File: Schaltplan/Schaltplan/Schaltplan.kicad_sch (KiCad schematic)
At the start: 32 parts, among them J1 Raspberry Pi Pico, M1 Motor_DC, M2 Motor_DC, M3 Motor_DC, M4 Motor_DC, M5 Motor_DC, Q1 IRLZ44N, Q2 IRLZ44N, Q3 IRLZ44N, Q4 IRLZ44N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

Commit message: j
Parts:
- removed R11: 10k, symbol Device:R
- R10, R6, R7, R8, R9: value 1k -> 330
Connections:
- net +12V: now also D1.1 (K), D2.1 (K), D3.1 (K), D4.1 (K), D5.1 (K); no longer D1.2 (A), D2.2 (A), D3.2 (A), D4.2 (A), D5.2 (A)
- net GND: now also J1.18 (Pin_35), Q1.3 (S), Q2.2 (D), Q3.2 (D), Q4.2 (D), Q5.2 (D), SW_Füllstand_1.2 (B), SW_Füllstand_2.2 (B), SW_Füllstand_3.2 (B), SW_Füllstand_4.2 (B), SW_Füllstand_5.2 (B)
- net at R1.1, R2.1, R3.1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: now also J1.36 (Pin_10); no longer J1.39 (Pin_4)
- net at M3.2 (-), Q3.1 (G): now also D3.2 (A); no longer D3.1 (K)
- net at M5.2 (-), Q5.1 (G): now also D5.2 (A); no longer D5.1 (K)
- net at M2.2 (-), Q2.1 (G): now also D2.2 (A); no longer D2.1 (K)
- net at M4.2 (-), Q4.1 (G): now also D4.2 (A); no longer D4.1 (K)
- net at R6.2: now also Q1.1 (G); no longer Q1.3 (S)
- new net: D1.2 (A), M1.2 (-), Q1.2 (D)
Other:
- moved on the sheet: D1, D2, D3, D4, D5, Q1
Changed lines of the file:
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@@
 	)
 	(junction
+		(at 180.34 71.12)
+		(diameter 0)
+		(color 0 0 0 0)
+	)
+	(junction
 		(at 267.97 20.32)
 		(diameter 0)
@@
 	)
 	(junction
-		(at 180.34 71.12)
-		(diameter 0)
-		(color 0 0 0 0)
-	)
-	(junction
 		(at 270.51 20.32)
 		(diameter 0)
@@
 	(wire
 		(pts
-			(xy 165.1 38.1) (xy 224.79 38.1)
+			(xy 167.64 38.1) (xy 224.79 38.1)
 		)
 		(stroke
@@
 	(wire
 		(pts
+			(xy 110.49 52.07) (xy 118.11 52.07)
+		)
+		(stroke
+			(width 0)
+			(type default)
+		)
+	)
+	(wire
+		(pts
 			(xy 180.34 129.54) (xy 180.34 151.13)
 		)
@@
 	(wire
 		(pts
+			(xy 170.18 71.12) (xy 180.34 71.12)
+		)
+		(stroke
+			(width 0)
+			(type default)
+		)
+	)
+	(wire
+		(pts
 			(xy 19.05 59.69) (xy 19.05 74.93)
 		)
@@
 	(wire
 		(pts
-			(xy 227.33 62.23) (xy 165.1 62.23)
+			(xy 167.64 53.34) (xy 167.64 52.07)
 		)
 		(stroke
@@
 	(wire
 		(pts
-			(xy 121.92 80.01) (xy 121.92 129.54)
+			(xy 227.33 62.23) (xy 165.1 62.23)
 		)
 		(stroke
@@
 	(wire
 		(pts
-			(xy 19.05 25.4) (xy 19.05 41.91)
+			(xy 121.92 80.01) (xy 121.92 129.54)
 		)
 		(stroke
@@
 	(wire
 		(pts
-			(xy 240.03 119.38) (xy 240.03 116.84)
+			(xy 19.05 25.4) (xy 19.05 41.91)
 		)
 		(stroke
@@
 	(wire
 		(pts
-			(xy 240.03 119.38) (xy 223.52 119.38)
+			(xy 240.03 119.38) (xy 240.03 116.84)
 		)
 		(stroke
@@
 	(wire
 		(pts
-			(xy 227.33 45.72) (xy 227.33 49.53)
+			(xy 240.03 119.38) (xy 223.52 119.38)
 		)
 		(stroke
@@
 	(wire
 		(pts
-			(xy 110.49 44.45) (xy 118.11 44.45)
+			(xy 227.33 45.72) (xy 227.33 49.53)
 		)
 		(stroke
@@
 	(wire
 		(pts
-			(xy 165.1 38.1) (xy 165.1 39.37)
+			(xy 167.64 38.1) (xy 167.64 41.91)
 		)
 		(stroke
@@
 	(wire
 		(pts
-			(xy 180.34 46.99) (xy 180.34 71.12)
+			(xy 180.34 53.34) (xy 180.34 71.12)
 		)
 		(stroke
@@
 	(wire
 		(pts
-			(xy 180.34 46.99) (xy 170.18 46.99)
+			(xy 180.34 53.34) (xy 167.64 53.34)
 		)
 		(stroke
@@
 	(wire
 		(pts
-			(xy 180.34 160.02) (xy 199.39 160.02)
+			(xy 180.34 160.02) (xy 246.38 160.02)
 		)
 		(stroke
@@
 	(wire
 		(pts
-			(xy 207.01 160.02) (xy 246.38 160.02)
-		)
-		(stroke
-			(width 0)
-			(type default)
-		)
-	)
-	(wire
-		(pts
 			(xy 224.79 38.1) (xy 240.03 38.1)
 		)
@@
 	(wire
 		(pts
-			(xy 118.11 44.45) (xy 118.11 25.4)
+			(xy 118.11 25.4) (xy 118.11 52.07)
 		)
 		(stroke
@@
 	(wire
 		(pts
-			(xy 180.34 71.12) (xy 170.18 71.12)
-		)
-		(stroke
-			(width 0)
-			(type default)
-		)
-	)
-	(wire
-		(pts
 			(xy 240.03 20.32) (xy 240.03 24.13)
 		)
@@
 	(symbol
 		(lib_id "Device:D")
-		(at 224.79 81.28 90)
+		(at 224.79 81.28 270)
 		(unit 1)
 		(exclude_from_sim no)
@@
 		(fields_autoplaced yes)
 		(property "Reference" "D3"
-			(at 218.44 81.28 0)
+			(at 227.33 80.0099 90)
 			(effects
 				(font
 					(size 1.27 1.27)
 				)
+				(justify left)
 			)
 		)
 		(property "Value" "D"
-			(at 220.98 81.28 0)
+			(at 227.33 82.5499 90)
 			(effects
 				(font
 					(size 1.27 1.27)
 				)
+				(justify left)
 			)
 		)
@@
 			)
 		)
-		(property "Value" "1k"
+		(property "Value" "330"
 			(at 138.43 67.31 90)
 			(effects
@@
 	(symbol
 		(lib_id "Device:D")
-		(at 222.25 134.62 90)
+		(at 222.25 134.62 270)
 		(unit 1)
 		(exclude_from_sim no)
@@
 		(fields_autoplaced yes)
 		(property "Reference" "D5"
-			(at 215.9 134.62 0)
+			(at 224.79 133.3499 90)
 			(effects
 				(font
 					(size 1.27 1.27)
 				)
+				(justify left)
 			)
 		)
 		(property "Value" "D"
-			(at 218.44 134.62 0)
+			(at 224.79 135.8899 90)
 			(effects
 				(font
 					(size 1.27 1.27)
 				)
+				(justify left)
 			)
 		)
@@
 	)
 	(symbol
-		(lib_id "Device:R")
-		(at 203.2 160.02 90)
-		(unit 1)
-		(exclude_from_sim no)
-		(in_bom yes)
-		(on_board yes)
-		(dnp no)
-		(fields_autoplaced yes)
-		(property "Reference" "R11"
-			(at 203.2 153.67 90)
-			(effects
-				(font
-					(size 1.27 1.27)
-				)
-			)
-		)
-		(property "Value" "10k"
-			(at 203.2 156.21 90)
-			(effects
-				(font
-					(size 1.27 1.27)
-				)
-			)
-		)
-		(property "Footprint" ""
-			(at 203.2 161.798 90)
-			(effects
-				(font
-					(size 1.27 1.27)
-				)
-				(hide yes)
-			)
-		)
-		(property "Datasheet" "~"
-			(at 203.2 160.02 0)
-			(effects
-				(font
-					(size 1.27 1.27)
-				)
-				(hide yes)
-			)
-		)
-		(property "Description" "Resistor"
-			(at 203.2 160.02 0)
-			(effects
-				(font
-					(size 1.27 1.27)
-				)
-				(hide yes)
-			)
-		)
-		(pin "2"
-		)
-		(pin "1"
-		)
-		(instances
-			(project "Schaltplan"
-				(path "/0e7ac635-20e1-4295-a698-68ba131a98e3"
-					(reference "R11")
-					(unit 1)
-				)
-			)
-		)
-	)
-	(symbol
 		(lib_id "Switch:SW_SPST")
 		(at 57.15 55.88 0)
@@
 			)
 		)
-		(property "Value" "1k"
+		(property "Value" "330"
 			(at 138.43 147.32 90)
 			(effects
@@
 			)
 		)
-		(property "Value" "1k"
+		(property "Value" "330"
 			(at 138.43 43.18 90)
 			(effects
@@
 	(symbol
 		(lib_id "Device:D")
-		(at 223.52 109.22 90)
+		(at 223.52 109.22 270)
 		(unit 1)
 		(exclude_from_sim no)
@@
 		(fields_autoplaced yes)
 		(property "Reference" "D4"
-			(at 217.17 109.22 0)
+			(at 226.06 107.9499 90)
 			(effects
 				(font
 					(size 1.27 1.27)
 				)
+				(justify left)
 			)
 		)
 		(property "Value" "D"
-			(at 219.71 109.22 0)
+			(at 226.06 110.4899 90)
 			(effects
 				(font
 					(size 1.27 1.27)
 				)
+				(justify left)
 			)
 		)
@@
 	(symbol
 		(lib_id "Device:D")
-		(at 227.33 53.34 90)
+		(at 227.33 53.34 270)
 		(unit 1)
 		(exclude_from_sim no)
@@
 		(fields_autoplaced yes)
 		(property "Reference" "D2"
-			(at 220.98 53.34 0)
+			(at 229.87 52.0699 90)
 			(effects
 				(font
 					(size 1.27 1.27)
 				)
+				(justify left)
 			)
 		)
 		(property "Value" "D"
-			(at 223.52 53.34 0)
+			(at 229.87 54.6099 90)
 			(effects
 				(font
 					(size 1.27 1.27)
 				)
+				(justify left)
 			)
 		)
@@
 	(symbol
 		(lib_id "Transistor_FET:IRLZ44N")
-		(at 165.1 44.45 270)
+		(at 165.1 46.99 0)
 		(unit 1)
 		(exclude_from_sim no)
@@
 		(fields_autoplaced yes)
 		(property "Reference" "Q1"
-			(at 165.1 50.8 90)
+			(at 171.45 45.7199 0)
 			(effects
 				(font
 					(size 1.27 1.27)
 				)
+				(justify left)
 			)
 		)
 		(property "Value" "IRLZ44N"
-			(at 165.1 53.34 90)
+			(at 171.45 48.2599 0)
 			(effects
 				(font
 					(size 1.27 1.27)
 				)
+				(justify left)
 			)
 		)
 		(property "Footprint" "Package_TO_SOT_THT:TO-220-3_Vertical"
-			(at 163.195 49.53 0)
+			(at 170.18 48.895 0)
 			(effects
 				(font
@@
 		)
 		(property "Datasheet" "http://www.irf.com/product-info/datasheets/data/irlz44n.pdf"
-			(at 161.29 49.53 0)
+			(at 170.18 50.8 0)
 			(effects
 				(font
@@
 		)
 		(property "Description" "47A Id, 55V Vds, 22mOhm Rds Single N-Channel HEXFET Power MOSFET, TO-220AB"
-			(at 165.1 44.45 0)
+			(at 165.1 46.99 0)
 			(effects
 				(font
@@
 			)
 		)
-		(property "Value" "1k"
+		(property "Value" "330"
 			(at 138.43 96.52 90)
 			(effects
@@
 			)
 		)
-		(property "Value" "1k"
+		(property "Value" "330"
 			(at 138.43 125.73 90)
 			(effects
@@
 	(symbol
 		(lib_id "Device:D")
-		(at 224.79 31.75 90)
+		(at 224.79 31.75 270)
 		(unit 1)
 		(exclude_from_sim no)
@@
 					(size 1.27 1.27)
 				)
-				(justify right)
+				(justify left)
 			)
 		)
@@
 					(size 1.27 1.27)
 				)
-				(justify right)
+				(justify left)
 			)
 		)

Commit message: hardware, mixer controller, rating
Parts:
- M1: value Motor_DC -> Wasser
- M2: value Motor_DC -> Sirup a
- M3: value Motor_DC -> Sirup b
- M4: value Motor_DC -> Sirup c
- M5: value Motor_DC -> Alkohol
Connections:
- net GND: now also Q2.3 (S), Q3.3 (S), Q4.3 (S), Q5.3 (S); no longer Q2.2 (D), Q3.2 (D), Q4.2 (D), Q5.2 (D)
- net at D3.2 (A), M3.2 (-): now also Q3.2 (D); no longer Q3.1 (G)
- net at R7.2: now also Q2.1 (G); no longer Q2.3 (S)
- net at D5.2 (A), M5.2 (-): now also Q5.2 (D); no longer Q5.1 (G)
- net at D2.2 (A), M2.2 (-): now also Q2.2 (D); no longer Q2.1 (G)
- net at R10.2: now also Q5.1 (G); no longer Q5.3 (S)
- net at R8.2: now also Q3.1 (G); no longer Q3.3 (S)
- net at D4.2 (A), M4.2 (-): now also Q4.2 (D); no longer Q4.1 (G)
- net at R9.2: now also Q4.1 (G); no longer Q4.3 (S)
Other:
- moved on the sheet: Q2, Q3, Q4, Q5, R9

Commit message: sensor test
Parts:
- removed J1: Raspberry Pi Pico, symbol Connector_Generic:Conn_02x20_Odd_Even
- removed SW_Füllstand_1, SW_Füllstand_2, SW_Füllstand_3, SW_Füllstand_4, SW_Füllstand_5: SW_SPST, symbol Switch:SW_SPST
- added C: Raspberry Pi Pico, symbol Connector_Generic:Conn_02x20_Odd_Even
- added H1, H2, H3, H4, H5: ~, symbol Connector_Generic_MountingPin:Conn_2Rows-11Pins_MountingPin
- added R11, R12, R13, R14, R15: 1kOhm, symbol Device:R
- added S1, S2, S3, S4, S5: Sensor, symbol Connector:Conn_01x04_Pin
- R1, R2, R3, R4, R5: value 10k -> 1kOhm
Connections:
- net GND: now also C.GND (Pin_36), H1.GND (Pin_2), H2.GND (Pin_2), H3.GND (Pin_2), H4.GND (Pin_2), H5.GND (Pin_2)
- net at R5.2: now also H3.A- (Pin_5), R11.2
- net at R1.2: now also R2.2, H1.A- (Pin_5)
- net at R10.1: now also C.GP18 (Pin_34)
- net at R9.1: now also C.GP19 (Pin_32)
- net at R8.1: now also C.GP20 (Pin_30)
- net at R7.1: now also C.GP21 (Pin_28)
- net at R6.1: now also C.GP22 (Pin_24)
- net at R3.2: now also R4.2, H2.A- (Pin_5)
- new net: H3.A+ (Pin_7), S3.RD (Pin_3)
- new net: C.GP3 (Pin_9), H3.DT (Pin_4)
- new net: H3.E+, H3.E- (Pin_3), R11.1, R5.1, S3.BL (Pin_2), S3.WH (Pin_1)
- new net: C.GP0 (Pin_1), H1.SCK (Pin_6), H2.SCK (Pin_6), H3.SCK (Pin_6), H4.SCK (Pin_6), H5.SCK (Pin_6)
- new net: C.3V3 (Pin_10), H1.VCC (Pin_8), H2.VCC (Pin_8), H3.VCC (Pin_8), H4.VCC (Pin_8), H5.VCC (Pin_8)
- new net: H5.E- (Pin_3), R14.1, S5.BL (Pin_2)
- new net: H5.A- (Pin_5), R14.2, R15.2
- new net: H4.E+, H4.E- (Pin_3), R12.1, R13.1, S4.BL (Pin_2), S4.WH (Pin_1)
- new net: H4.A- (Pin_5), R12.2, R13.2
- new net: H5.A+ (Pin_7), S5.RD (Pin_3)
- new net: H5.E+, R15.1, S5.WH (Pin_1)
- new net: H2.A+ (Pin_7), S2.RD (Pin_3)
- new net: C.GP2 (Pin_7), H2.DT (Pin_4)
- new net: H2.E+, R4.1, S2.WH (Pin_1)
- new net: H2.E- (Pin_3), R3.1, S2.BL (Pin_2)
- new net: H1.E+, R2.1, S1.WH (Pin_1)
- new net: H4.A+ (Pin_7), S4.RD (Pin_3)
- new net: H1.E- (Pin_3), R1.1, S1.BL (Pin_2)
- new net: H1.A+ (Pin_7), S1.RD (Pin_3)
- new net: C.GP1 (Pin_3), H1.DT (Pin_4)
- new net: C.GP15 (Pin_39), C.GP16 (Pin_40)
- new net: C.GP4 (Pin_11), H4.DT (Pin_4)
- new net: C.GP5 (Pin_13), H5.DT (Pin_4)

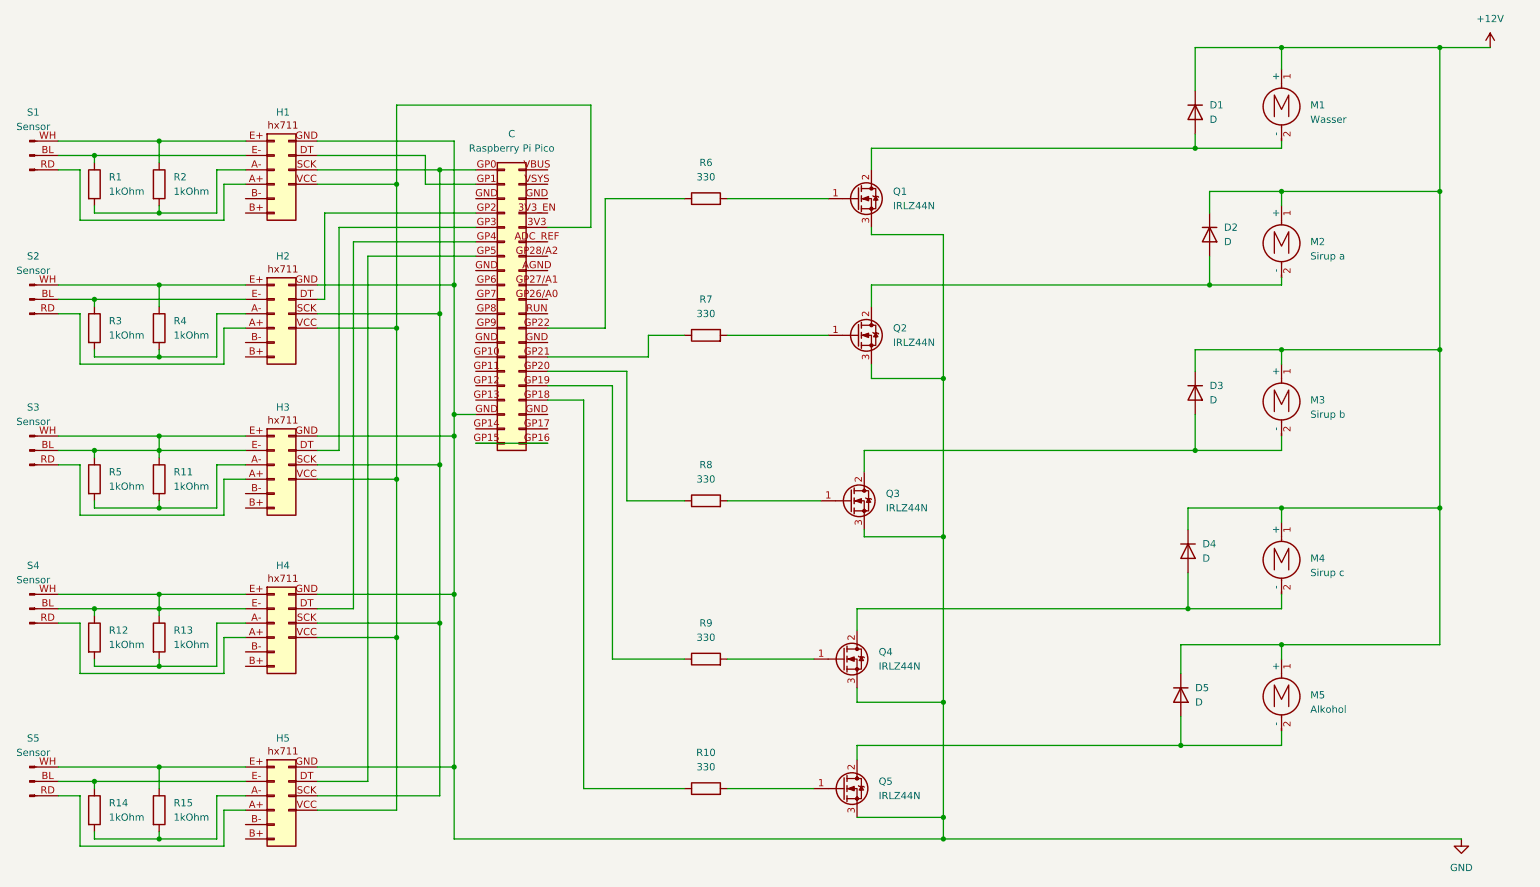
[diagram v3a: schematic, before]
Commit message: Implement basic functionality for beverage mixer including HX711 weight measurement and GPIO setup for pumps and sensors. Add initial test script for basic output.
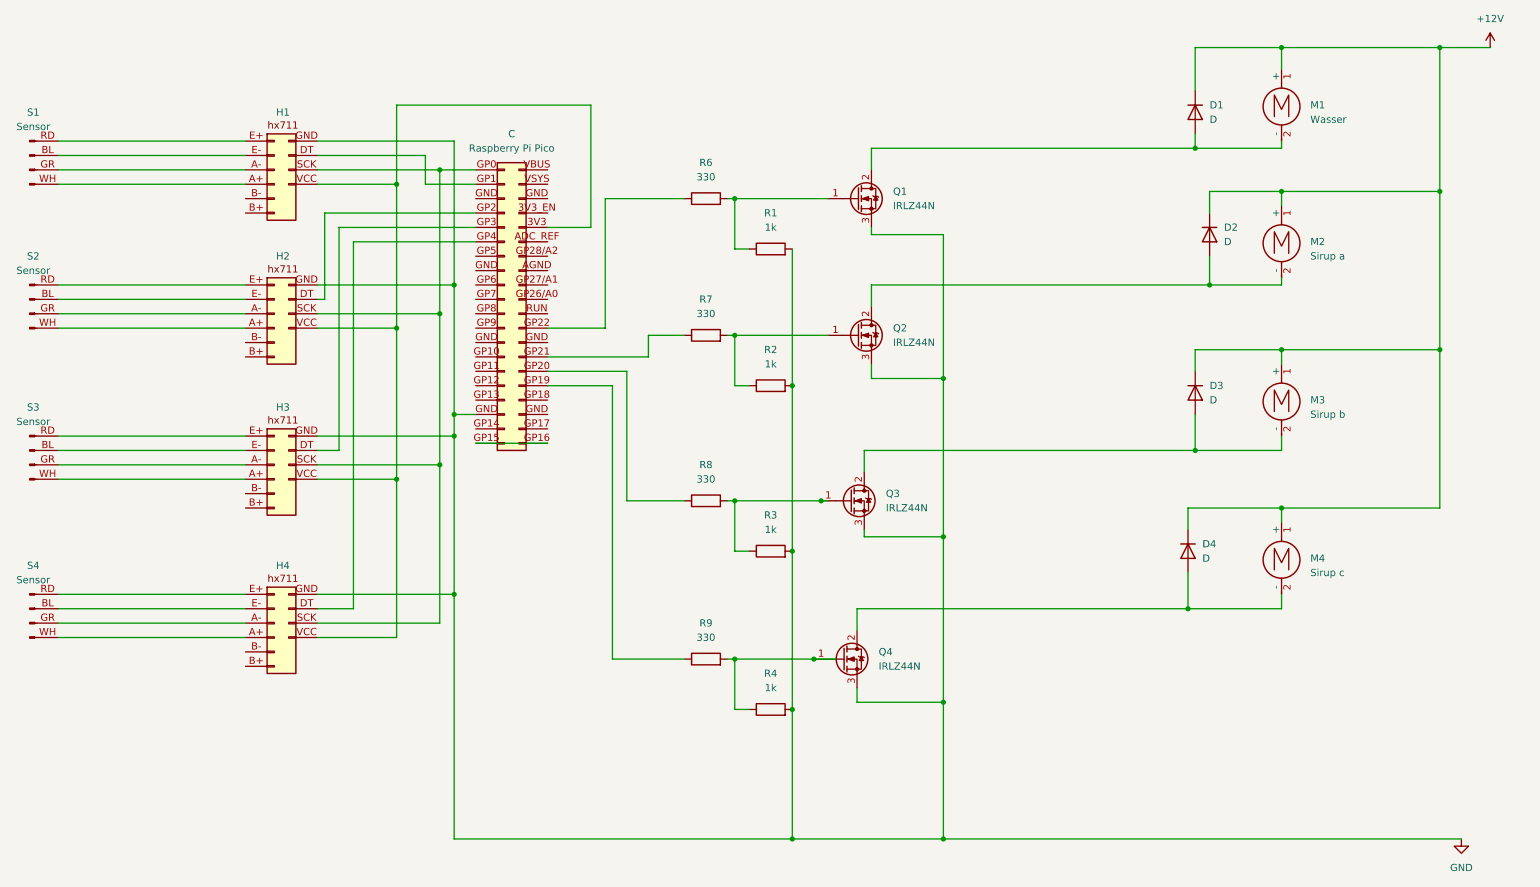
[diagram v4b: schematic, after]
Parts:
- removed D5: D, symbol Device:D
- removed H5: ~, symbol Connector_Generic_MountingPin:Conn_2Rows-11Pins_MountingPin
- removed M5: Alkohol, symbol Motor:Motor_DC
- removed Q5: IRLZ44N, Package_TO_SOT_THT:TO-220-3_Vertical, symbol Transistor_FET:IRLZ44N
- removed R10: 330, symbol Device:R
- removed R11, R12, R13, R14, R15, R5: 1kOhm, symbol Device:R
- removed S5: Sensor, symbol Connector:Conn_01x04_Pin
- R1, R2, R3, R4: value 1kOhm -> 1k
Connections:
- net GND: now also R1.2, R2.2, R3.2, R4.2
- net at Q2.1 (G), R7.2: now also R2.1
- net at H3.A+ (Pin_7): now also S3.WH (Pin_4); no longer S3.RD (Pin_3)
- net at H3.A- (Pin_5): now also S3.GR (Pin_3)
- net at H3.E- (Pin_3), S3.BL (Pin_2): no longer H3.E+, S3.WH (Pin_1)
- net at H4.E- (Pin_3), S4.BL (Pin_2): no longer H4.E+, S4.WH (Pin_1)
- net at H4.A- (Pin_5): now also S4.GR (Pin_3)
- net at H2.A+ (Pin_7): now also S2.WH (Pin_4); no longer S2.RD (Pin_3)
- net at H2.E- (Pin_3), S2.BL (Pin_2): no longer R3.1
- net at H4.A+ (Pin_7): now also S4.WH (Pin_4); no longer S4.RD (Pin_3)
- net at Q3.1 (G), R8.2: now also R3.1
- net at H1.E- (Pin_3), S1.BL (Pin_2): no longer R1.1
- net at S1.RD (Pin_1): now also H1.E+; no longer H1.A+ (Pin_7)
- net at Q4.1 (G), R9.2: now also R4.1
- net at Q1.1 (G), R6.2: now also R1.1
- new net: H3.E+, S3.RD (Pin_1)
- new net: H2.A- (Pin_5), S2.GR (Pin_3)
- new net: H2.E+, S2.RD (Pin_1)
- new net: H1.A- (Pin_5), S1.GR (Pin_3)
- new net: H1.A+ (Pin_7), S1.WH (Pin_4)
- new net: H4.E+, S4.RD (Pin_1)
